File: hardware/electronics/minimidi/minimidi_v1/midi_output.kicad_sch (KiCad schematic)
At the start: 7 parts, among them J11-O1 SJ-3524-SMT

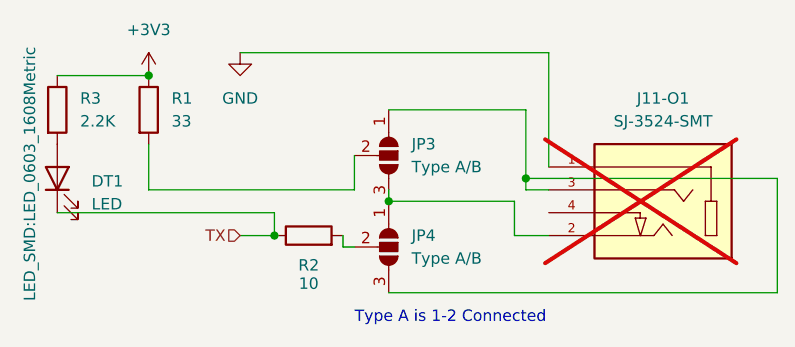
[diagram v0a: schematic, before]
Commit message: Rework schemas with JLCPCB references
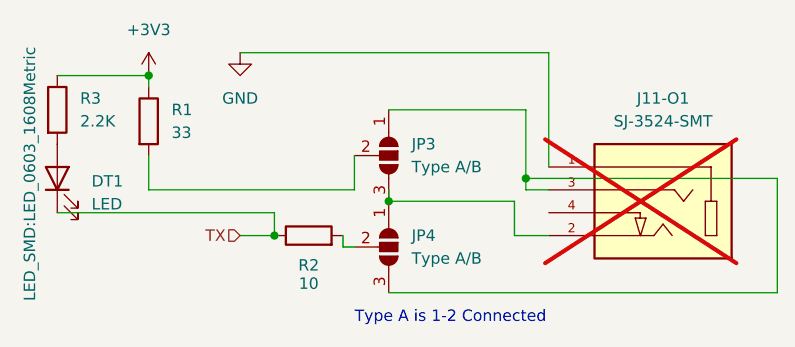
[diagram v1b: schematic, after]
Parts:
- R1: footprint Resistor_SMD:R_1206_3216Metric_Pad1.30x1.75mm_HandSolder -> Resistor_SMD:R_0805_2012Metric; LCSC C137308 -> C17634
- R2: footprint Resistor_SMD:R_1206_3216Metric_Pad1.30x1.75mm_HandSolder -> Resistor_SMD:R_0805_2012Metric; LCSC C140052 -> C17415
- R3: LCSC C441982 -> C17520
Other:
- moved on the sheet: R1
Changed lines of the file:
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@@
 	(wire
 		(pts
-			(xy 130.81 85.09) (xy 130.81 80.01)
+			(xy 130.81 85.09) (xy 130.81 81.28)
 		)
 		(stroke
@@
 		(pts
 			(xy 120.65 87.63) (xy 144.78 87.63)
+		)
+		(stroke
+			(width 0)
+			(type default)
+		)
+	)
+	(wire
+		(pts
+			(xy 130.81 73.66) (xy 130.81 72.39)
 		)
 		(stroke
@@
 			)
 		)
-		(property "LCSC" " C441982 "
+		(property "LCSC" "C17520"
 			(at 120.65 76.2 0)
 			(effects
@@
 	(symbol
 		(lib_id "Device:R")
-		(at 130.81 76.2 0)
+		(at 130.81 77.47 0)
 		(unit 1)
 		(exclude_from_sim no)
@@
 		(fields_autoplaced yes)
 		(property "Reference" "R1"
-			(at 133.35 74.9299 0)
+			(at 133.35 76.1999 0)
 			(effects
 				(font
@@
 		)
 		(property "Value" "33"
-			(at 133.35 77.4699 0)
+			(at 133.35 78.7399 0)
 			(effects
 				(font
@@
 			)
 		)
-		(property "Footprint" "Resistor_SMD:R_1206_3216Metric_Pad1.30x1.75mm_HandSolder"
-			(at 129.032 76.2 90)
+		(property "Footprint" "Resistor_SMD:R_0805_2012Metric"
+			(at 129.032 77.47 90)
 			(effects
 				(font
@@
 		)
 		(property "Datasheet" "~"
-			(at 130.81 76.2 0)
+			(at 130.81 77.47 0)
 			(effects
 				(font
@@
 		)
 		(property "Description" "Resistor"
-			(at 130.81 76.2 0)
-			(effects
-				(font
-					(size 1.27 1.27)
-				)
-				(hide yes)
-			)
-		)
-		(property "LCSC" "C137308 "
-			(at 130.81 76.2 0)
+			(at 130.81 77.47 0)
+			(effects
+				(font
+					(size 1.27 1.27)
+				)
+				(hide yes)
+			)
+		)
+		(property "LCSC" " C17634 "
+			(at 130.81 77.47 0)
 			(effects
 				(font
@@
 		(dnp no)
 		(fields_autoplaced yes)
-		(property "Reference" "#PWR04"
+		(property "Reference" "#PWR010"
 			(at 140.97 76.2 0)
 			(effects
@@
 			)
 		)
-		(property "Footprint" "Resistor_SMD:R_1206_3216Metric_Pad1.30x1.75mm_HandSolder"
+		(property "Footprint" "Resistor_SMD:R_0805_2012Metric"
 			(at 148.59 91.948 90)
 			(effects
@@
 			)
 		)
-		(property "LCSC" "C140052"
+		(property "LCSC" "C17415 "
 			(at 148.59 90.17 90)
 			(effects
